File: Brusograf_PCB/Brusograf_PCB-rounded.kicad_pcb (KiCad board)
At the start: 2 copper layers, 159 x 48.8 mm, 40 parts, among them J1 Conn_01x05_Socket, J2 Conn_01x05_Socket, J3 Conn_01x05_Socket, J4 SD_Card_Receptacle, J5 Barrel_Jack_Switch, J6 Conn_01x07_Socket, J7 Conn_01x03_Pin, J8 Conn_01x01_Socket, U1 ULN2003A, U2 ULN2003A, U3 ULN2003A, U4 ESP32-DevKitC_mod

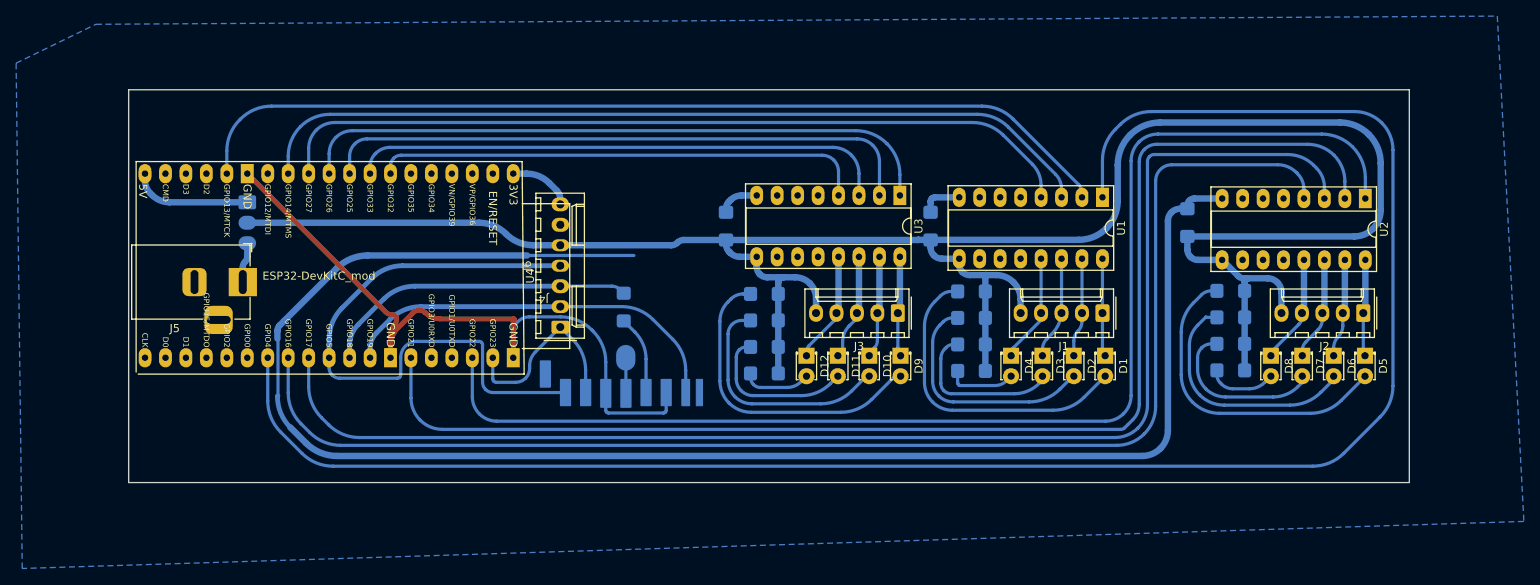
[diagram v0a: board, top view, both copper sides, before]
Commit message: fully manucturable PCB design and gerbers
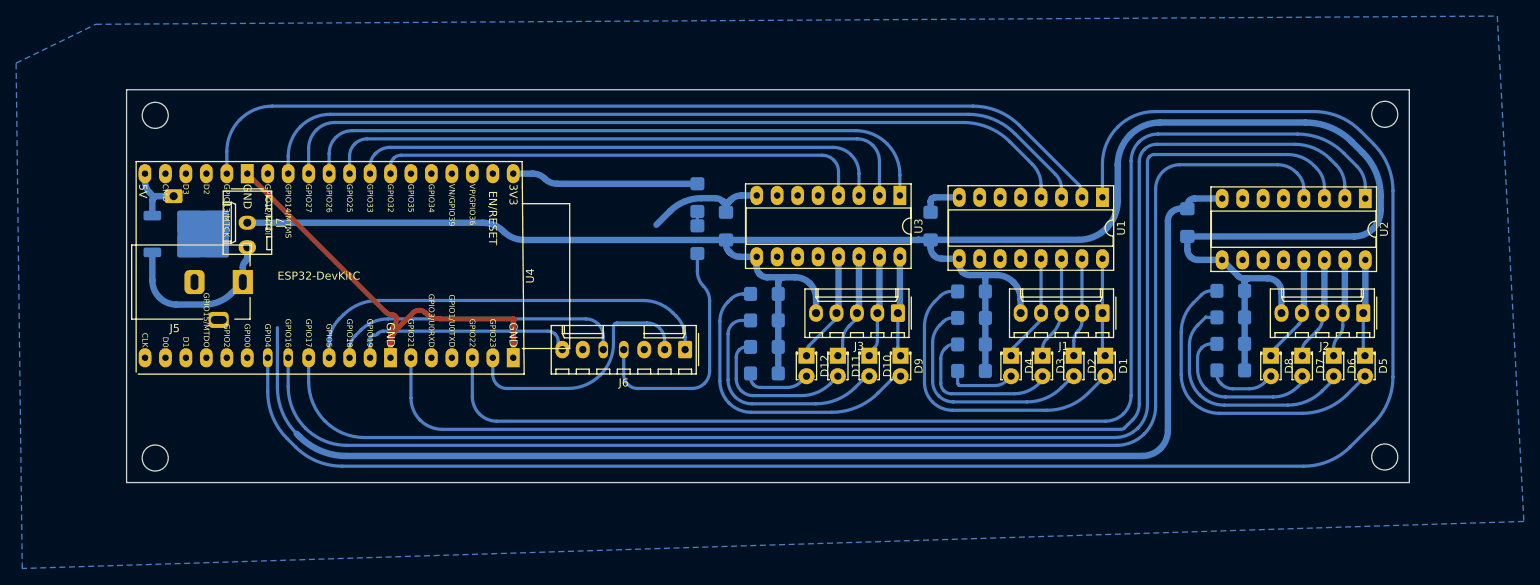
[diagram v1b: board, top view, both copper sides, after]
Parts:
- removed J4: SD_Card_Receptacle, Connector_Card:SD_Card_Device_16mm_SlotDepth
- removed J8: Conn_01x01_Socket, 007_dusjagr:SolderPad_small
- added R14: 0, 007_dusjagr:R_1206_noGND, B.Cu at (116.1, 98.7)
- added U5: L7805, Package_TO_SOT_SMD:TO-252-2, B.Cu at (53.5, 103.3)
- J6: footprint Connector_Molex:Molex_KK-254_AE-6410-07A_1x07_P2.54mm_Vertical -> 007_dusjagr:Molex_KK-254_AE-6410-07A_1x07_P2.54mm_Vertical
- J7: moved to F.Cu
- U4: value ESP32-DevKitC_mod -> ESP32-DevKitC
- moved J6 15.7 mm to (114.6, 117.6), turned to 180 degrees
- moved R13 12.4 mm to (116.1, 104.0)
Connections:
- J6 pad 1: MOSI -> CS
- J6 pad 2: MISO -> MOSI
- J6 pad 3: SCK -> GND
- J6 pad 4: CS -> Net-(J6-Pin_4)
- J6 pad 5: 5V -> SCK
- J6 pad 7: 3.3V -> MISO
- R13 pad 1: SCK -> Net-(R13-Pad1)
- R13 pad 2: Net-(J4-CLK) -> Net-(J6-Pin_4)
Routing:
- net GND: track 307.2 -> 235.8 mm
- net Net-(J6-Pin_4): track 0.00 -> 30.9 mm
- net CS: track 75.9 -> 52.6 mm
- net MISO: track 49.6 -> 28.0 mm
- net 5V-EXT: track 4.97 -> 22.3 mm
- net 3.3V: track 7.90 -> 23.2 mm
- net Net-(J4-CLK): track 9.81 -> 0.00 mm
- net MOSI: track 24.2 -> 32.2 mm
- net Net-(J7-Pin_1): track 15.0 -> 8.31 mm
- net Net-(J4-VDD): track 4.42 -> 0.00 mm
- net IN1_U1: track 230.1 -> 227.0 mm
- net 5V: track 276.0 -> 273.7 mm
- net SCK: track 39.4 -> 37.2 mm
- net Net-(R13-Pad1): track 0.00 -> 1.78 mm
- net IN1_U2: track 155.8 -> 154.7 mm
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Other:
- board size 159 x 48.8 mm -> 159.3 x 48.8 mm
